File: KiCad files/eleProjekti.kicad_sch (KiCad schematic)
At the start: 46 parts, among them J1 USB_C_Receptacle_USB2.0_16P, SW1 RESET, SW2 BOOT, U1 ESP32-S3-WROOM-1, U2 USBLC6-2SC6, U3 LM1117DT-ADJ, U4 BME280, U5 TPS63001, U6 TP4057, U7 TPS2116DRL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

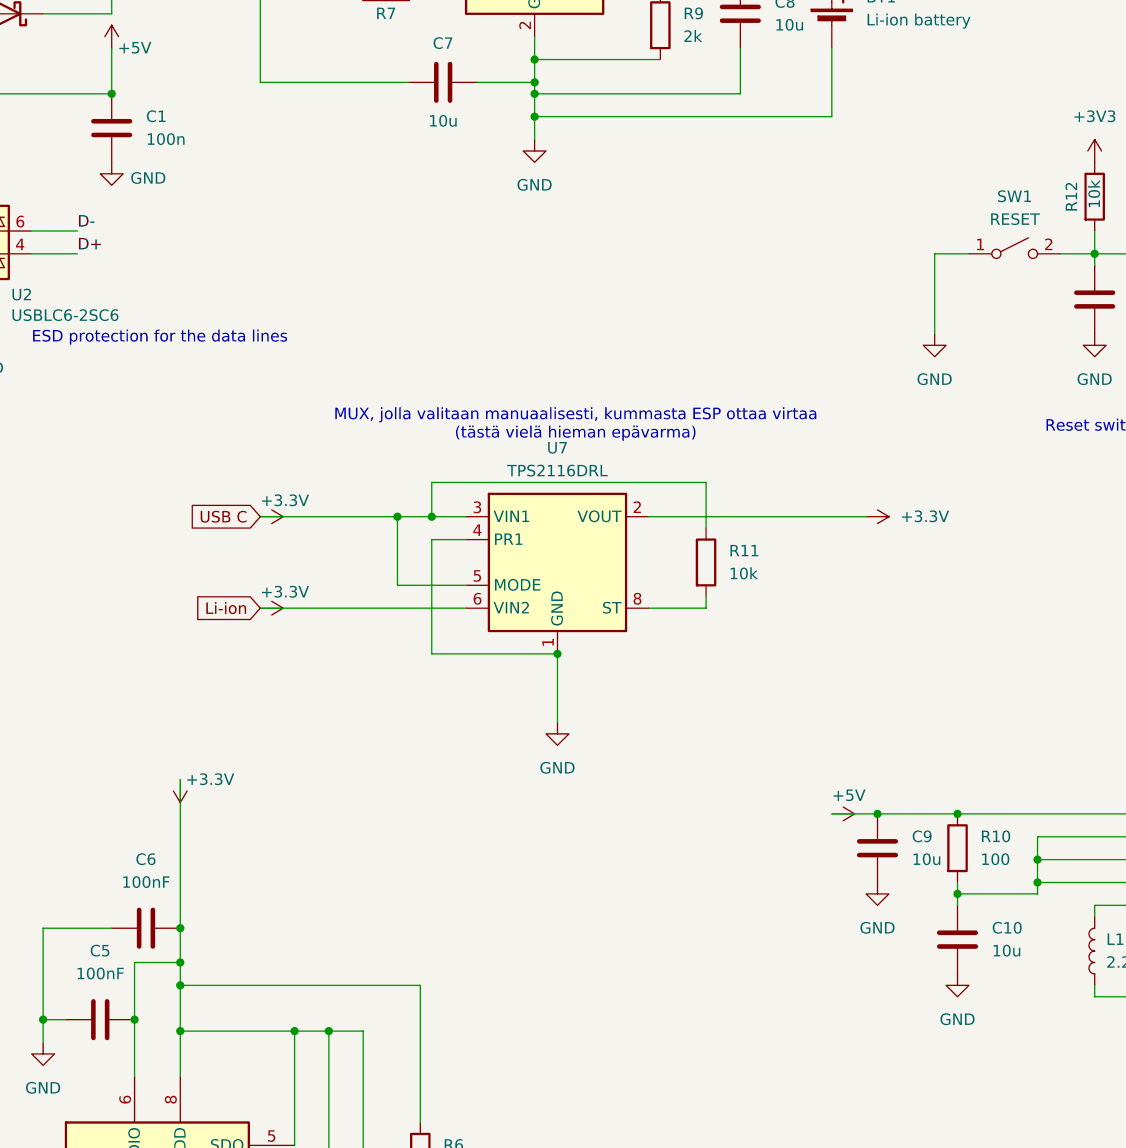
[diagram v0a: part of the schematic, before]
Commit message: Added expansion header schematic
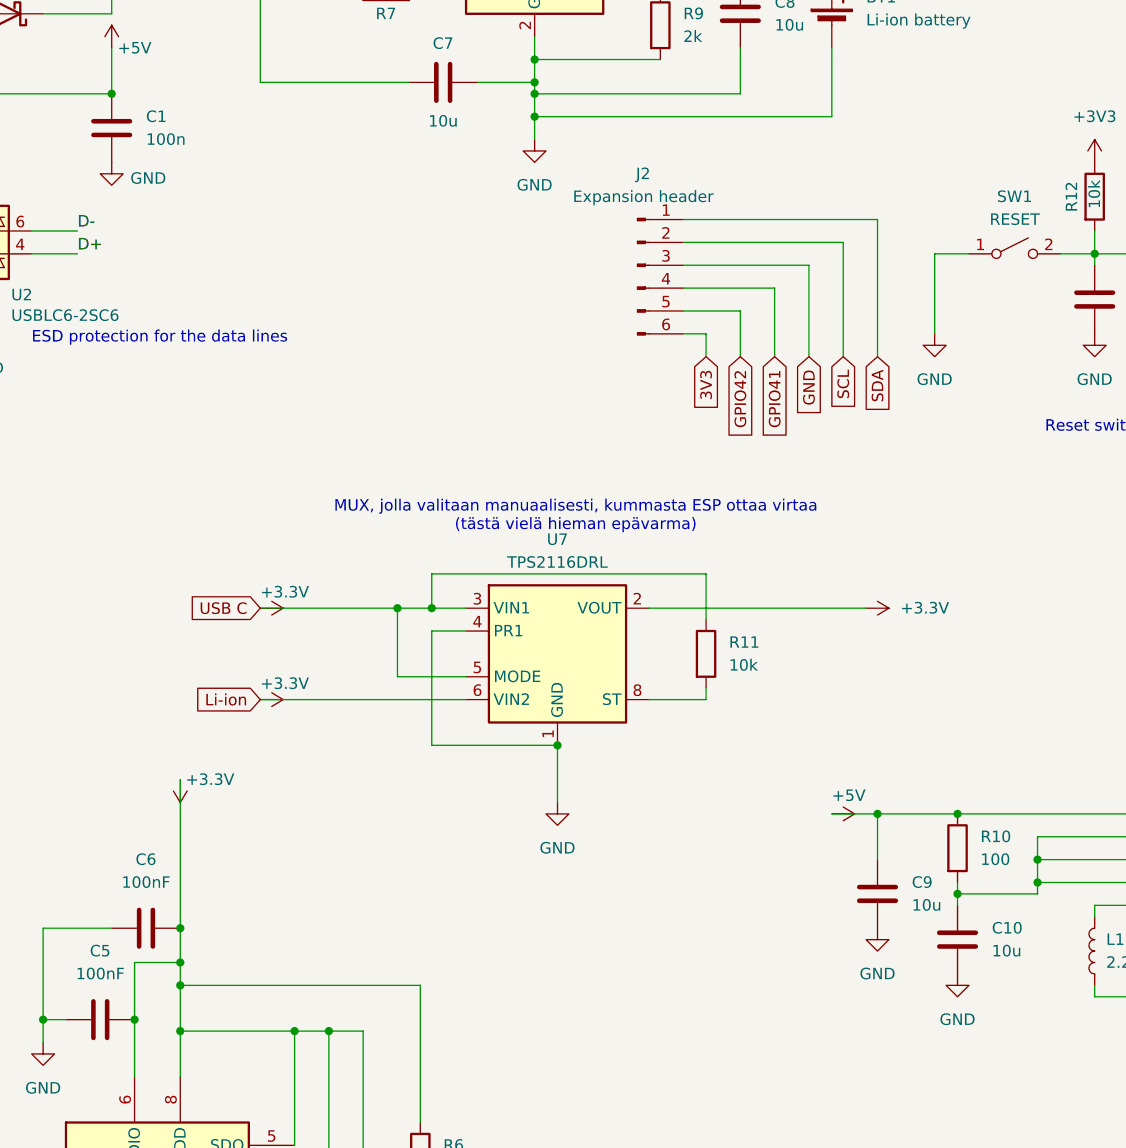
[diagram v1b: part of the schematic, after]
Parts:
- added J2: Expansion header, symbol Connector:Conn_01x06_Pin
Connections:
- net GND: now also J2.3 (Pin_3)
- net SCL: now also J2.2 (Pin_2)
- net SDA: now also J2.1 (Pin_1)
- new net 3V3: J2.6 (Pin_6)
- new net GPIO41: J2.4 (Pin_4)
- new net GPIO42: J2.5 (Pin_5)
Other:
- moved on the sheet: C9, R11, U7
